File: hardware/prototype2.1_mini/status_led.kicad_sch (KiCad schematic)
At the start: 0 parts

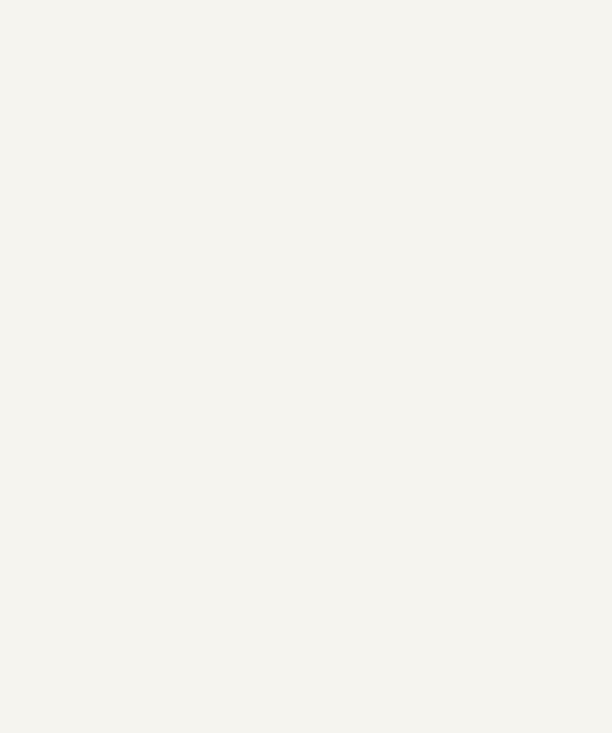
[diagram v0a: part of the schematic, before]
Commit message: fix LED footprint and mount 5 of them vertically
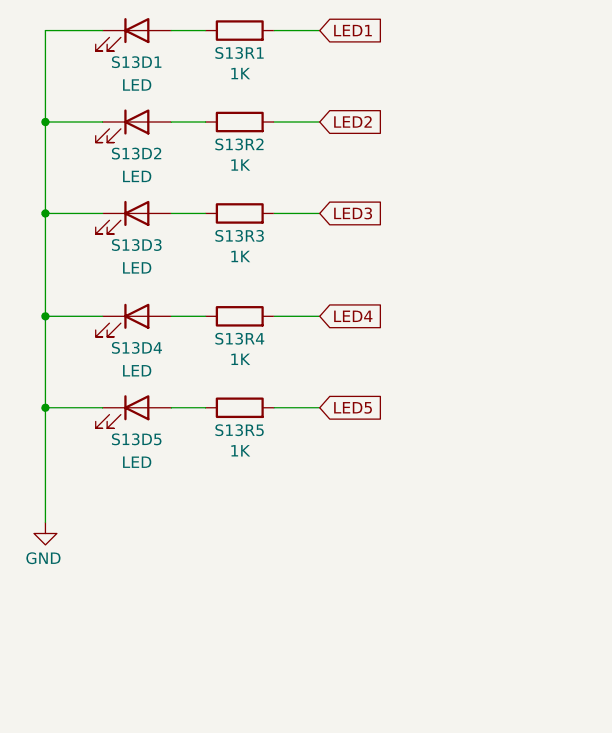
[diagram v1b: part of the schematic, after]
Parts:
- added S13D1, S13D2, S13D3, S13D4, S13D5: LED, LED_SMD:LED_0603_1608Metric, symbol Device:LED
- added S13R1, S13R2, S13R3, S13R4, S13R5: 1K, Resistor_SMD:R_0805_2012Metric, symbol Device:R
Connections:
- new net: S13D5.2 (A), S13R5.1
- new net: S13D1.2 (A), S13R1.1
- new net: S13D3.2 (A), S13R3.1
- new net: S13D2.2 (A), S13R2.1
- new net: S13D4.2 (A), S13R4.1
- new net GND: S13D1.1 (K), S13D2.1 (K), S13D3.1 (K), S13D4.1 (K), S13D5.1 (K)
- new net LED1: S13R1.2
- new net LED2: S13R2.2
- new net LED3: S13R3.2
- new net LED4: S13R4.2
- new net LED5: S13R5.2
